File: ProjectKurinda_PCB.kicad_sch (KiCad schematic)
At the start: 6 parts, among them J1 JST PH, U1 ESP32-C3_SUPERMINI_TH, U2 DHT11, U3 Water Sensor, U4 SD3031 RTC, U5 MPU6050

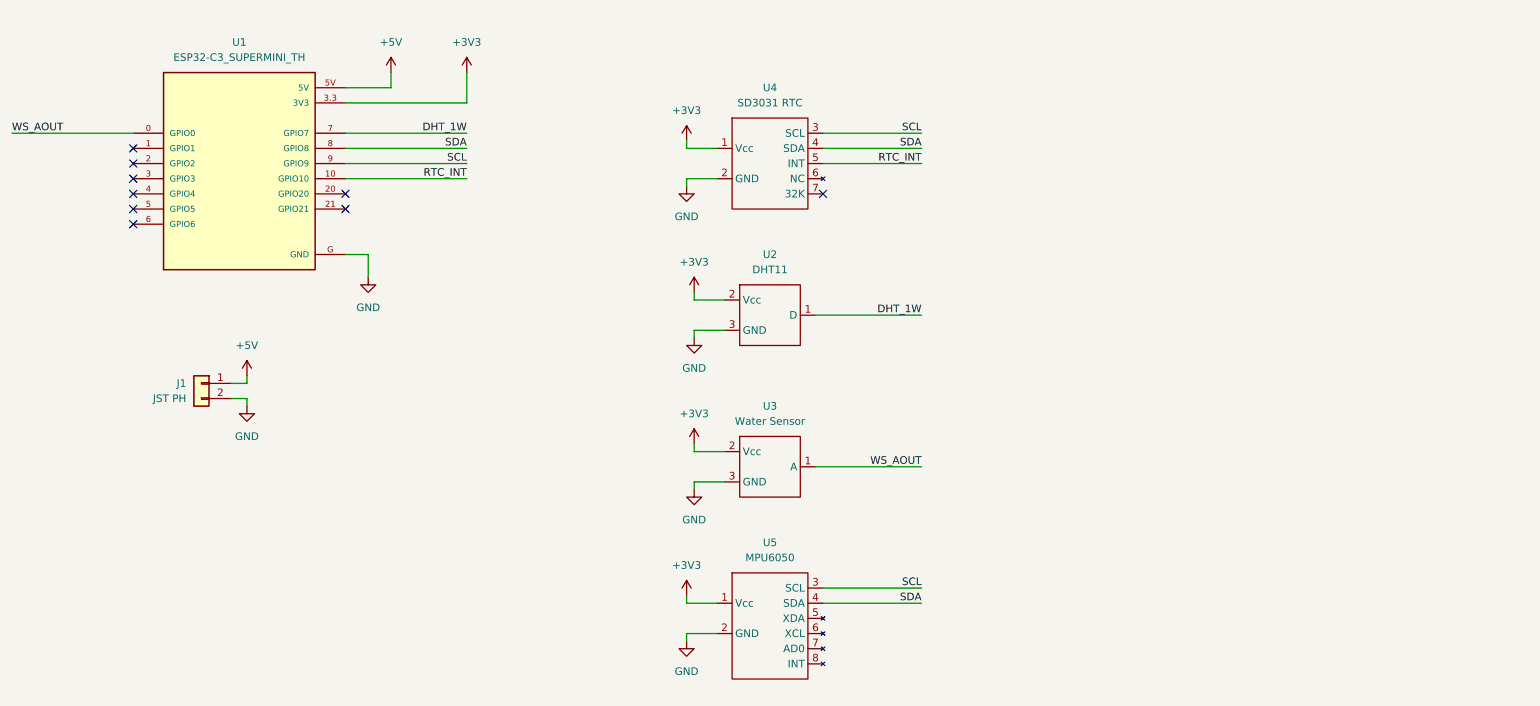
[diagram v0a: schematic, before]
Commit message: Added correct soil moisture sensor and updated silk screen to match.
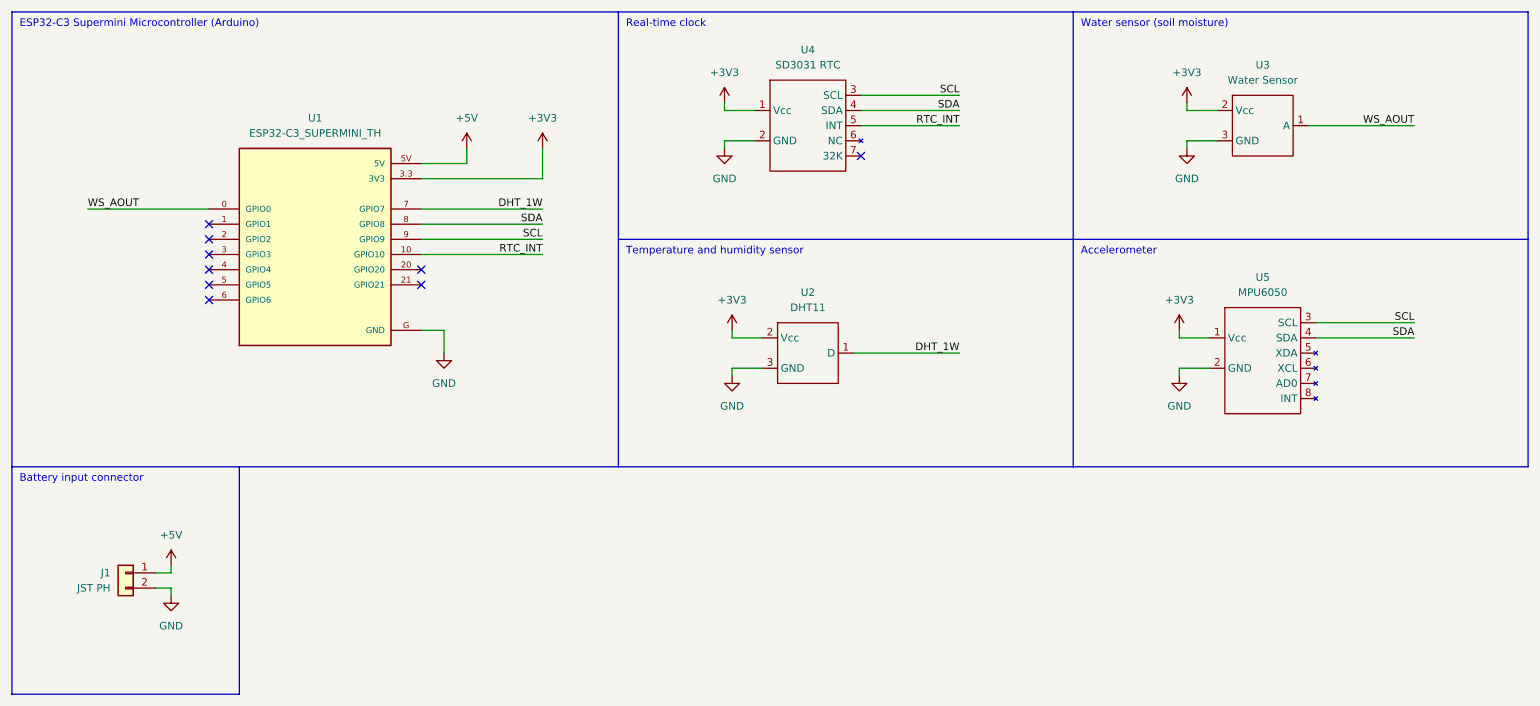
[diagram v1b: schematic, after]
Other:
- note added: "Accelerometer"
- note added: "Battery input connector"
- note added: "ESP32-C3 Supermini Microcontroller (Arduino)"
- note added: "Real-time clock"
- note added: "Temperature and humidity sensor"
- note added: "Water sensor (soil moisture)"
- title: (none) -> Project Kurinda Landslide Sensor (ESP32-C3)
- moved on the sheet: J1, U1, U2, U3, U4, U5
